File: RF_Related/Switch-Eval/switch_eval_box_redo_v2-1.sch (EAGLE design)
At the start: 20 parts, among them IC1 SN74LVC2G17DBVT, IC2 HSWA2-30DR+, IC4 MAX8878EUK28+T, J1 171856-0002, J2 M20-7830246, X1 SMA-142-0701-801/806, X2 SMA-142-0701-801/806, X3 SMA-142-0701-801/806

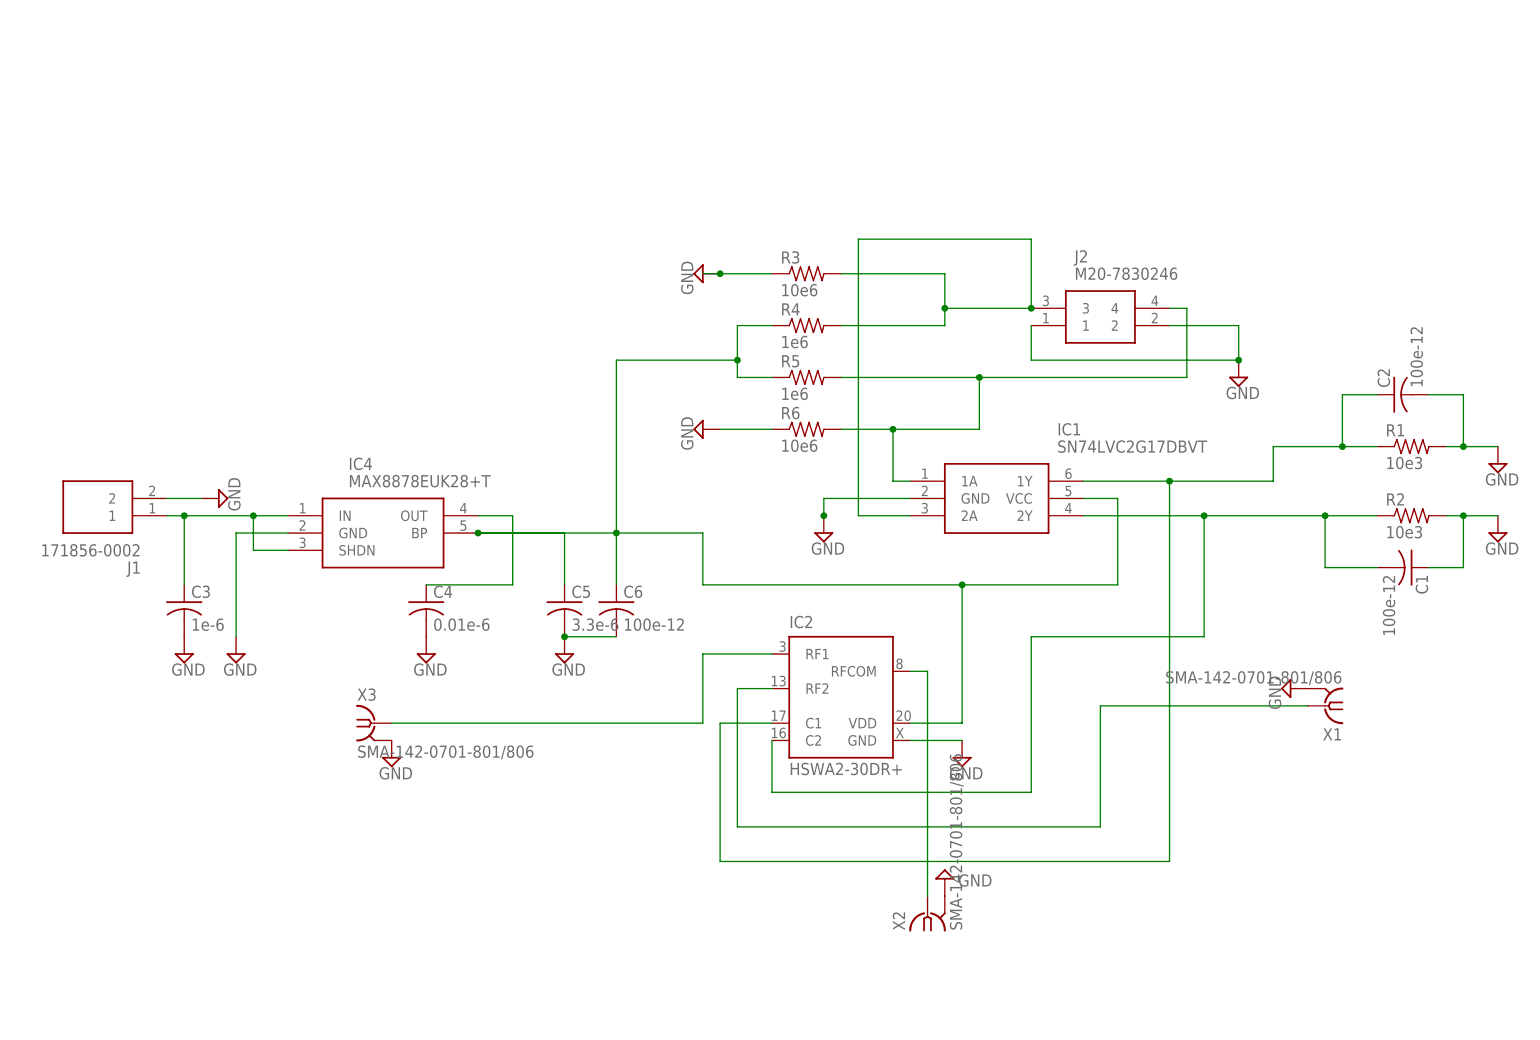
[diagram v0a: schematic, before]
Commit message: made a new revision of the simple RF switch and sent it to fab.
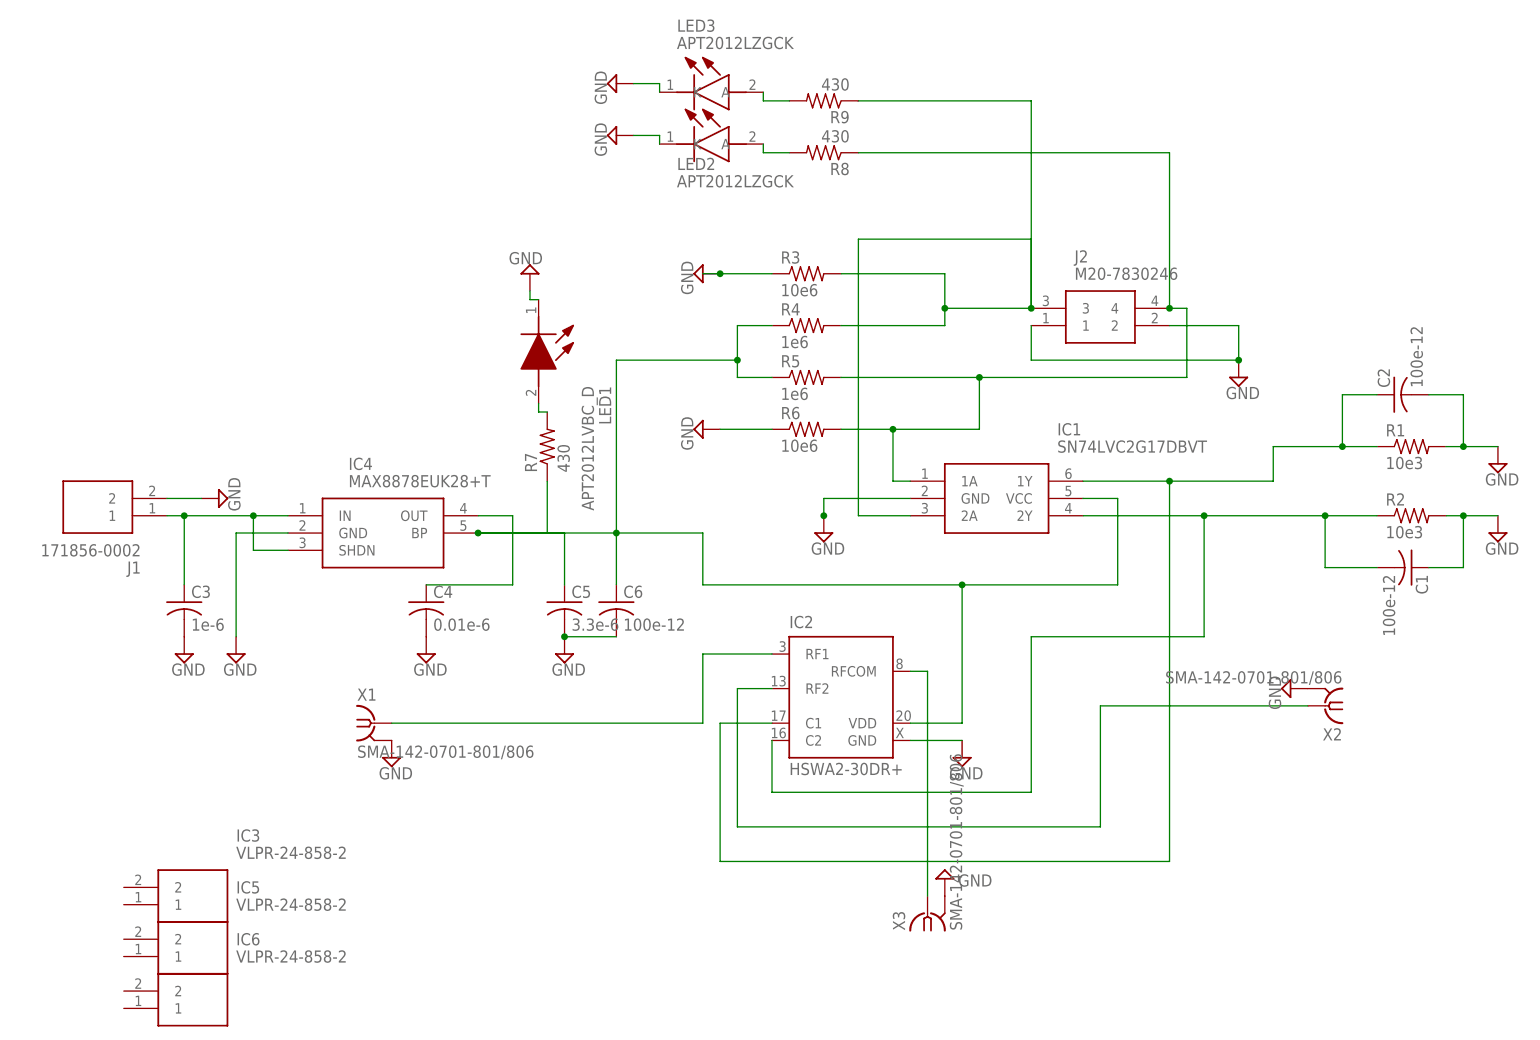
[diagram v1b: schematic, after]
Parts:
- added IC3, IC5, IC6: VLPR-24-858-2, VLPR-24-858-2:VLPR-24-858-2
- added LED1: APT2012LVBC_D, APT2012LVBC_D:APT2012LVBC_D
- added LED2, LED3: APT2012LZGCK, APT2012LZGCK:APT2012LZGCK
- added R7, R8, R9: 430, rcl:R-US_R0603
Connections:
- new net N$13: LED2.A, R8.2
- new net N$5: LED1.A, R7.2
- new net N$6: LED3.A, R9.2
- net GND: now also LED1.K, LED2.K, LED3.K
- net N$1: now also R9.1
- net N$10: now also X2.1; no longer X1.1
- net N$12: now also X3.1; no longer X2.1
- net N$4: now also R8.1
- net N$7: now also R7.1
- net N$8: now also X1.1; no longer X3.1
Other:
- moved on the sheet: X1, X2, X3
